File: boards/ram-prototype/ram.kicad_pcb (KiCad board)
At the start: 4 copper layers, 165 x 141 mm, 630 parts, among them J1 PinHeader_1x24_P2.54mm_Vertic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, J2 PinHeader_1x04_P2.54mm_Vertic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, J3 PinHeader_1x14_P2.54mm_Vertic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, J4 PinHeader_1x16_P2.54mm_Vertic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, J5 Molex_Mini-Fit_Jr_5566-08A_2x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, U1 DSBGA\-5_NumericPads, U10 DSBGA\-5_NumericPads, U100 DSBGA\-5_NumericPads, U101 DSBGA\-5_NumericPads, U102 DSBGA\-5_NumericPads, U103 DSBGA\-5_NumericPads, U104 DSBGA\-5_NumericPads, U105 DSBGA\-5_NumericPads, U106 DSBGA\-5_NumericPads, U107 DSBGA\-5_NumericPads, U108 DSBGA\-5_NumericPads, U109 DSBGA\-5_NumericPads, U11 DSBGA\-5_NumericPads, U110 DSBGA\-5_NumericPads, U111 DSBGA\-5_NumericPads, U112 DSBGA\-5_NumericPads, U113 DSBGA\-5_NumericPads, U114 DSBGA\-5_NumericPads, U115 DSBGA\-5_NumericPads, U116 DSBGA\-5_NumericPads, U117 DSBGA\-5_NumericPads, U118 DSBGA\-5_NumericPads, U119 DSBGA\-5_NumericPads, U12 DSBGA\-5_NumericPads, U120 DSBGA\-5_NumericPads, U121 DSBGA\-5_NumericPads, U122 DSBGA\-5_NumericPads, U123 DSBGA\-5_NumericPads, U124 DSBGA\-5_NumericPads, U125 DSBGA\-5_NumericPads, U126 DSBGA\-5_NumericPads, U127 DSBGA\-5_NumericPads, U128 DSBGA\-5_NumericPads, U129 DSBGA\-5_NumericPads, U13 DSBGA\-5_NumericPads, U130 DSBGA\-5_NumericPads, U131 DSBGA\-5_NumericPads, U132 DSBGA\-5_NumericPads, U133 DSBGA\-5_NumericPads, U134 DSBGA\-5_NumericPads, U135 DSBGA\-5_NumericPads, U136 DSBGA\-5_NumericPads, U137 DSBGA\-5_NumericPads, U138 DSBGA\-5_NumericPads, U139 DSBGA\-5_NumericPads, U14 DSBGA\-5_NumericPads, U140 DSBGA\-5_NumericPads, U141 DSBGA\-5_NumericPads, U142 DSBGA\-5_NumericPads, U143 DSBGA\-5_NumericPads, U144 DSBGA\-5_NumericPads, U145 DSBGA\-5_NumericPads, U146 DSBGA\-5_NumericPads, U147 DSBGA\-5_NumericPads, U148 DSBGA\-5_NumericPads, U149 DSBGA\-5_NumericPads, U15 DSBGA\-5_NumericPads, U150 DSBGA\-5_NumericPads, U151 DSBGA\-5_NumericPads, U152 DSBGA\-5_NumericPads, U153 DSBGA\-5_NumericPads, U154 DSBGA\-5_NumericPads, U155 DSBGA\-5_NumericPads, U156 DSBGA\-5_NumericPads, U157 DSBGA\-5_NumericPads, U158 DSBGA\-5_NumericPads, U159 DSBGA\-5_NumericPads, U16 DSBGA\-5_NumericPads, U160 DSBGA\-5_NumericPads, U161 DSBGA\-5_NumericPads, U162 DSBGA\-5_NumericPads, U163 DSBGA\-5_NumericPads, U164 DSBGA\-5_NumericPads, U165 DSBGA\-5_NumericPads, U166 DSBGA\-5_NumericPads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

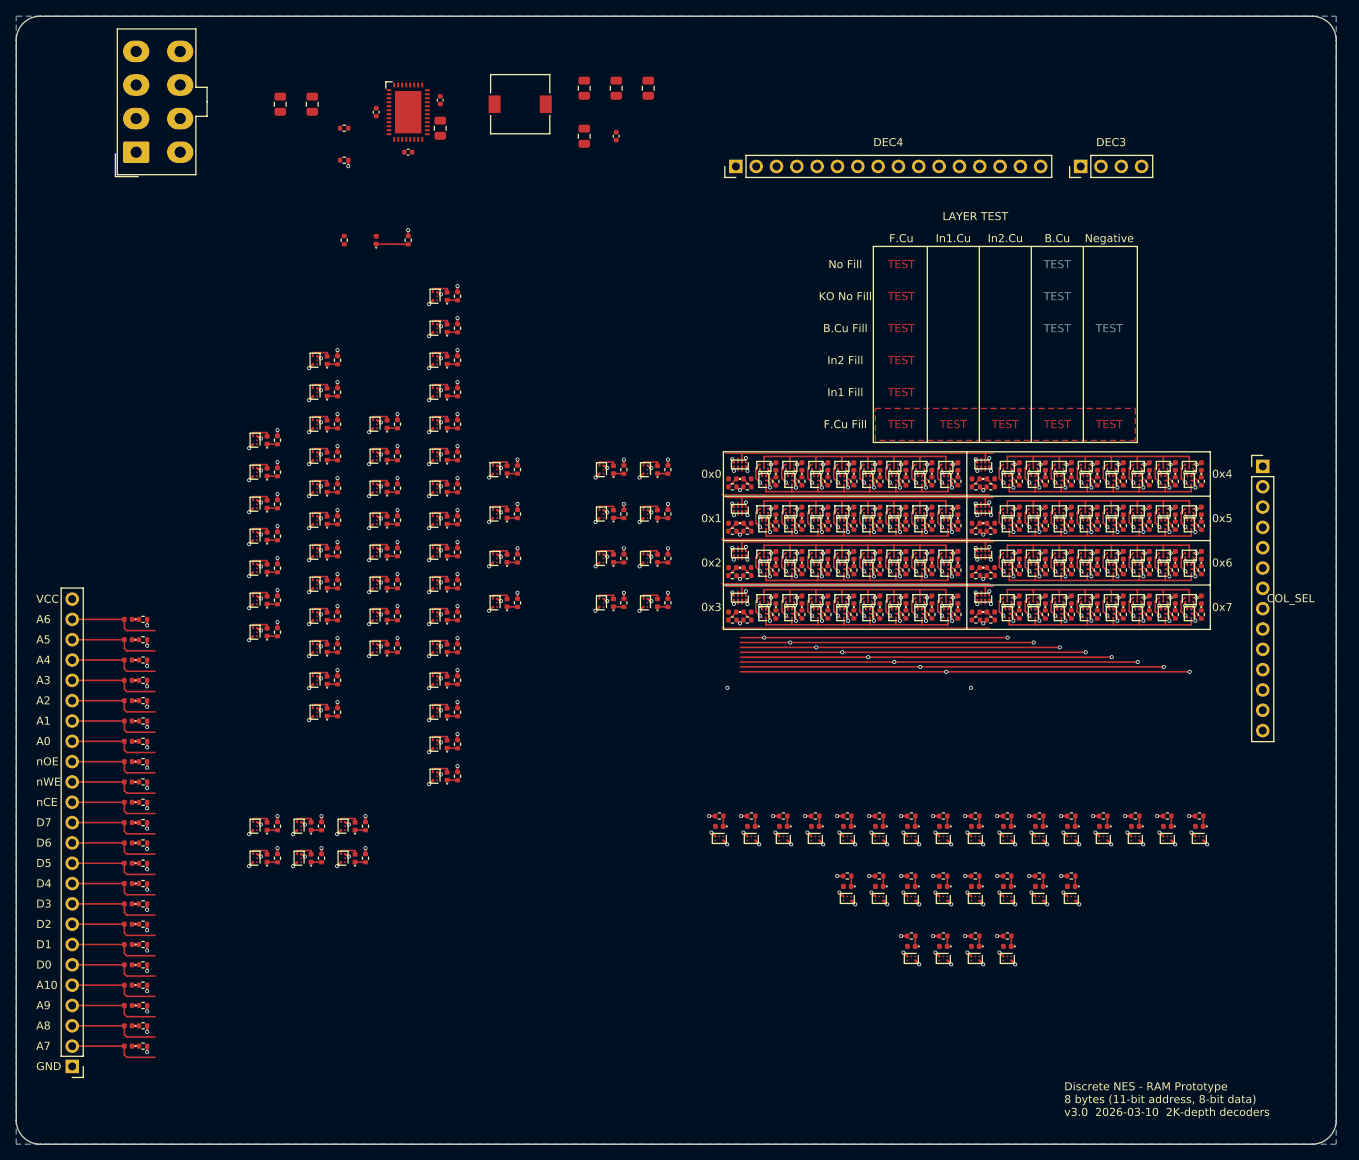
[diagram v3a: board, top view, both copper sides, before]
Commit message: add copper pours, thermal vias, and SW keepout for power supply layout
Rotates TPS546D24A 180° so PVIN faces input caps (left) and SW faces
inductor (right), matching datasheet layout recommendation (Fig 10-1).

Copper pours (F.Cu, regional):
- PVIN pour: input caps to PVIN pins, solid pad connection
- PGND pour: around thermal pad, connects vias to PGND pins
- VOUT pour: inductor output through output caps to VCC
- SW keepout zone: prevents fill in switching node area

Thermal vias: 2x3 grid (6 vias, 0.3mm drill) under exposed pad,
connecting F.Cu to B.Cu GND plane per datasheet land pattern.

Bypass caps repositioned for 180° IC rotation:
- C3 (PVIN HF) + C5 (VDD5): left side near respective pins
- C4 (BOOT) + C6 (BP1V5): right side near SW/BOOT area

Default DRC: 0 errors, 0 warnings.

Co-Authored-By: Claude Opus 4.6 (1M context) <noreply@anthropic.com>
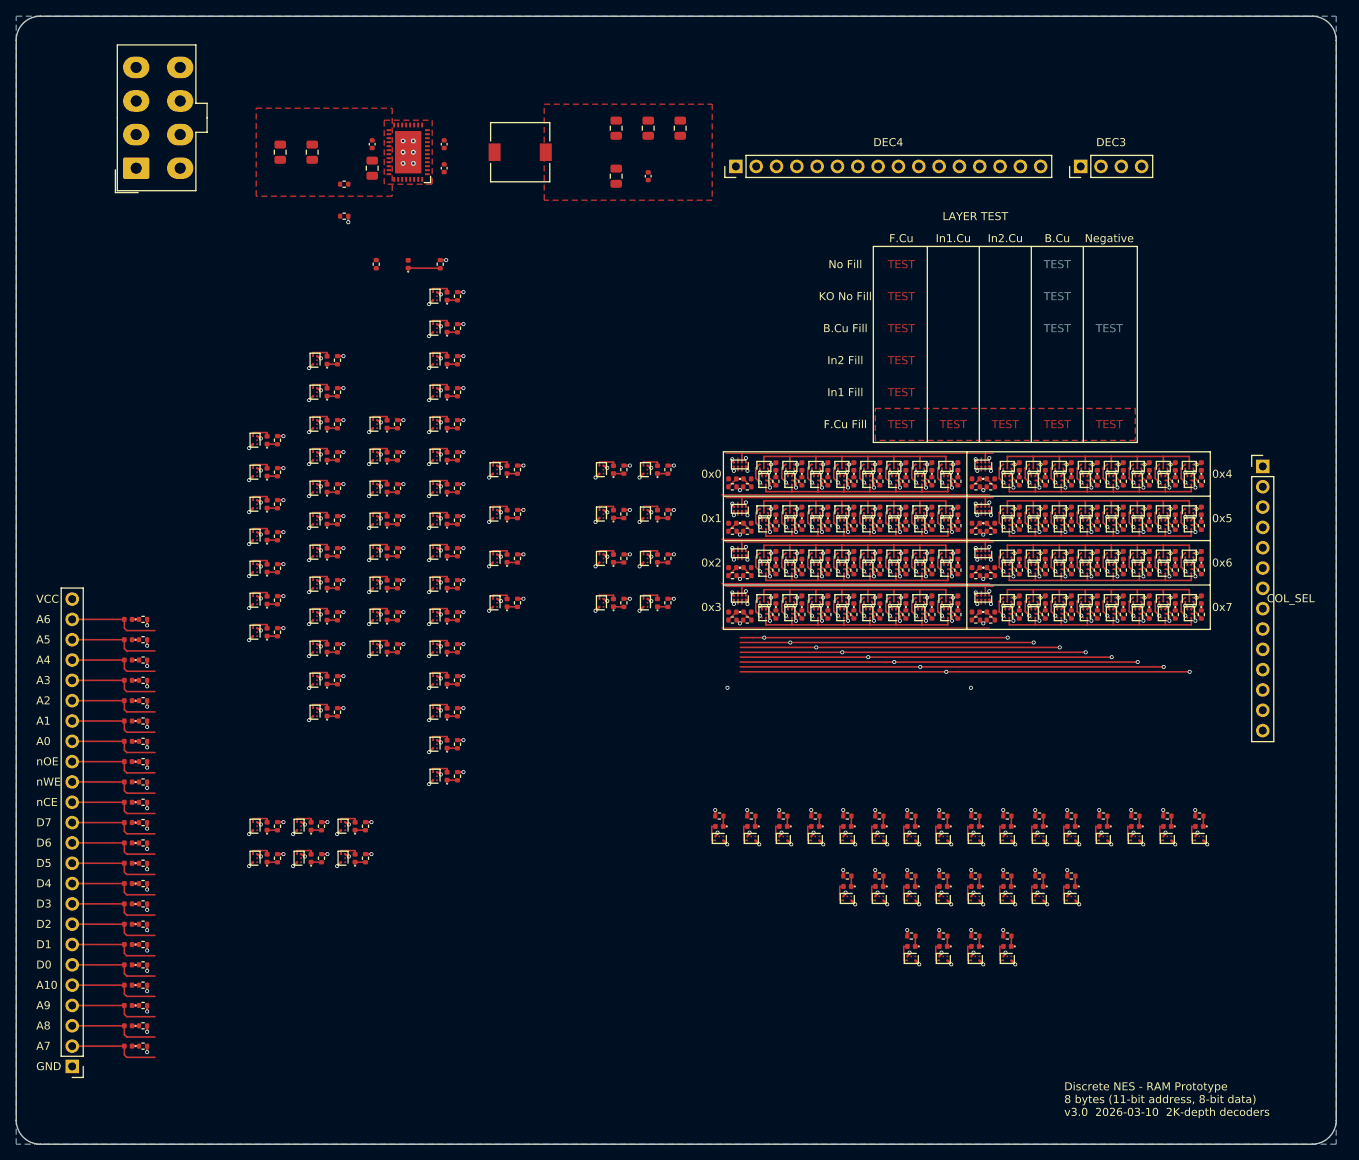
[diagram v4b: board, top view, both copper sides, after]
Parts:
- moved C5 9.86 mm to (57.5, 32.0)
- moved R192 7.00 mm to (54.0, 34.0)
- moved R193 7.00 mm to (54.0, 38.0)
- moved C10 6.40 mm to (88.0, 33.0)
- moved C11 6.40 mm to (92.0, 33.0)
- moved C7 6.40 mm to (88.0, 27.0)
- moved C8 6.40 mm to (92.0, 27.0)
- moved C9 6.40 mm to (96.0, 27.0)
- moved C1 6.00 mm to (46.0, 30.0)
- moved C2 6.00 mm to (50.0, 30.0)
- moved L1 6.00 mm to (76.0, 30.0)
- moved C4 5.52 mm to (66.5, 29.0)
- moved D192 5.00 mm to (62.0, 44.0)
- moved R194 5.00 mm to (58.0, 44.0)
- moved R195 5.00 mm to (66.0, 44.0)
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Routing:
- net GND: track 353.6 -> 349.7 mm, vias 282 -> 288
- net Net-(D70-A): track 0.00 -> 2.67 mm
- net /Column Select/GA2: track 0.00 -> 2.67 mm
- net /Column Select/GA1: track 0.00 -> 2.67 mm
- net /Column Select/GA0: track 0.00 -> 2.67 mm
- net /COL_SEL_6: track 0.00 -> 2.67 mm
- net /COL_SEL_5: track 0.00 -> 2.67 mm
- net /COL_SEL_4: track 0.00 -> 2.67 mm
- net /COL_SEL_3: track 0.00 -> 2.67 mm
- net /COL_SEL_2: track 0.00 -> 2.67 mm
- net /COL_SEL_1: track 43.6 -> 46.3 mm
- net /COL_SEL_0: track 43.6 -> 46.3 mm
- net Net-(D73-A): track 0.00 -> 2.66 mm
- net Net-(D72-A): track 0.00 -> 2.66 mm
- net Net-(D71-A): track 0.00 -> 2.66 mm
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- added copper zone on F.Cu, net /Power Supply/+12V
- added copper zone on F.Cu, net VCC

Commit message: stack row_ctrl write/read AND gates vertically with 45° enable bus routing
- Row control layout changed from side-by-side to vertically stacked
  (2.3mm spacing between write and read AND gate centers)
- WRITE_EN: 45° diagonal up-right from LED junction to bus
- READ_EN: corridor route (45° up-right, horizontal past R/GND via,
  45° diagonal down-right to bus)
- Row_ctrl-to-RAM gap reduced from 3.0mm to 1.0mm
- Board width reduced from 233mm to 158mm

Co-Authored-By: Claude Opus 4.6 (1M context) <noreply@anthropic.com>
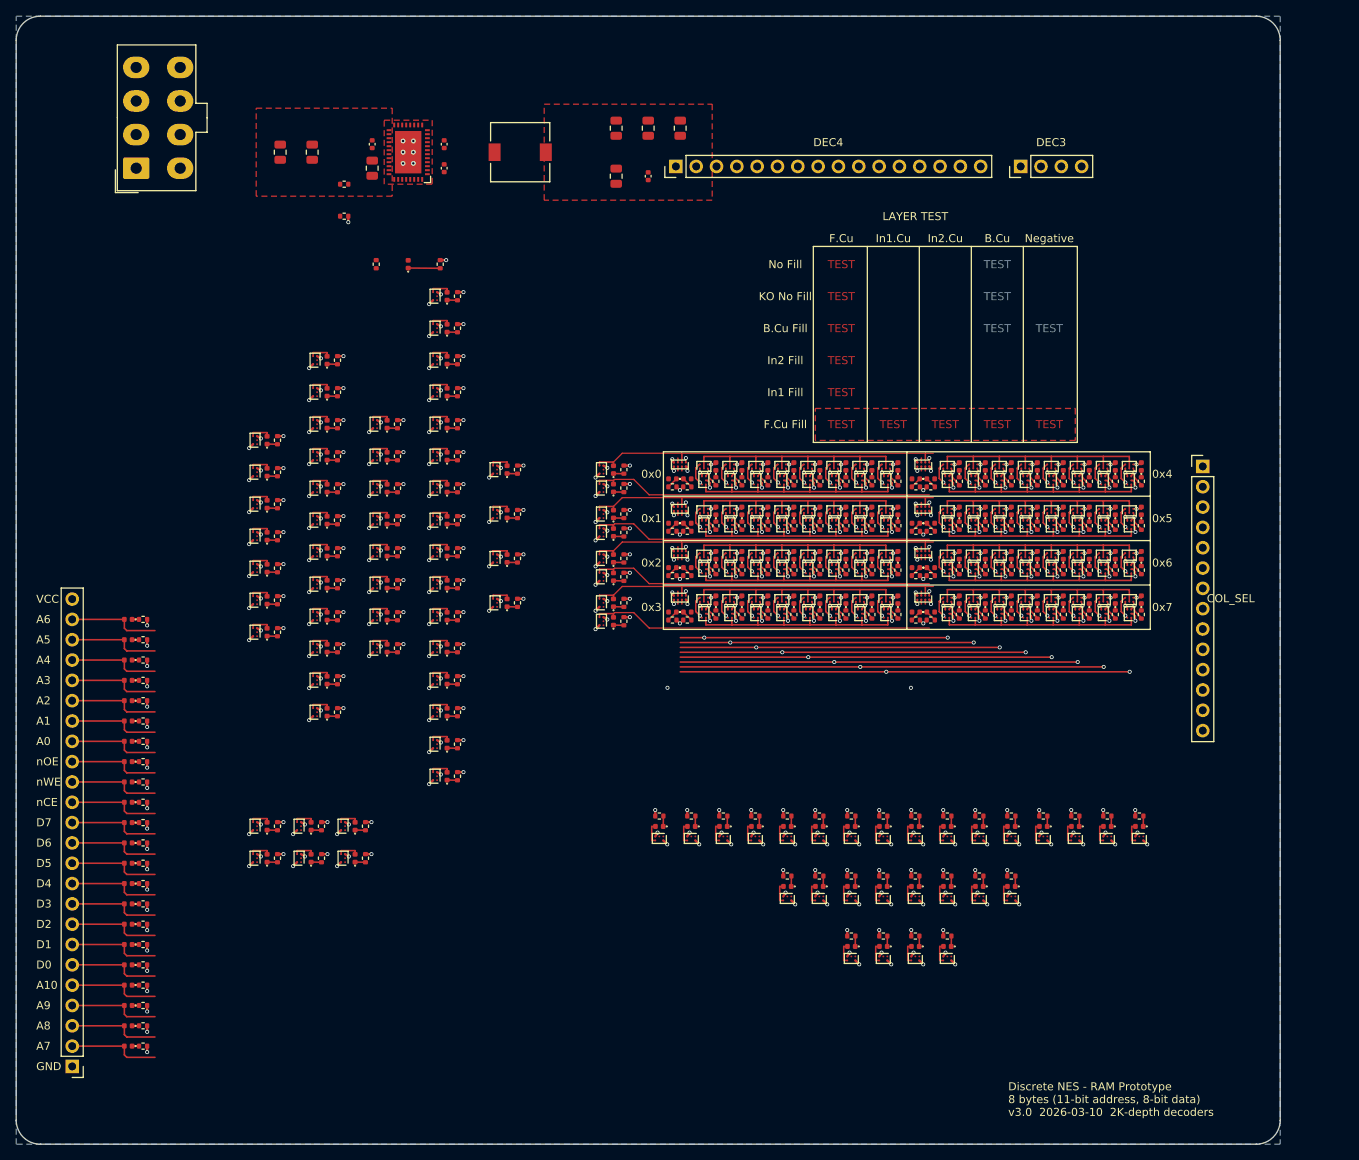
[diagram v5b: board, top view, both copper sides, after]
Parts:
- moved D124 7.50 mm to (125.5, 70.8)
- moved D125 7.50 mm to (125.5, 76.4)
- moved D126 7.50 mm to (125.5, 81.9)
- moved D127 7.50 mm to (125.5, 87.5)
- moved D128 7.50 mm to (123.2, 69.3)
- moved D129 7.50 mm to (123.2, 74.8)
- moved D130 7.50 mm to (123.2, 80.4)
- moved D131 7.50 mm to (123.2, 85.9)
- moved R124 7.50 mm to (125.5, 71.8)
- moved R125 7.50 mm to (125.5, 77.4)
- moved R126 7.50 mm to (125.5, 82.9)
- moved R127 7.50 mm to (125.5, 88.5)
- moved R128 7.50 mm to (123.2, 71.1)
- moved R129 7.50 mm to (123.2, 76.7)
- moved R130 7.50 mm to (123.2, 82.2)
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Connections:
- net /Power Supply/BOOT_INT renamed Net-(U226-BOOT)
- net /Power Supply/BP1V5_INT renamed Net-(U226-BP1V5)
- net /Power Supply/PGOOD renamed Net-(D192-A)
- net /Power Supply/VDD5_INT renamed Net-(U226-VDD5)
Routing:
- net /WRITE_EN_ROW_0: track 38.4 -> 45.4 mm
- net /WRITE_EN_ROW_3: track 38.4 -> 45.4 mm
- net /WRITE_EN_ROW_2: track 38.4 -> 45.4 mm
- net /WRITE_EN_ROW_1: track 38.4 -> 45.4 mm
- net /READ_EN_ROW_1: track 37.2 -> 44.1 mm
- net /READ_EN_ROW_0: track 37.2 -> 44.1 mm
- net /READ_EN_ROW_3: track 37.2 -> 44.1 mm
- net /READ_EN_ROW_2: track 37.2 -> 44.1 mm
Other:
- board size 165 x 141 mm -> 158 x 141 mm

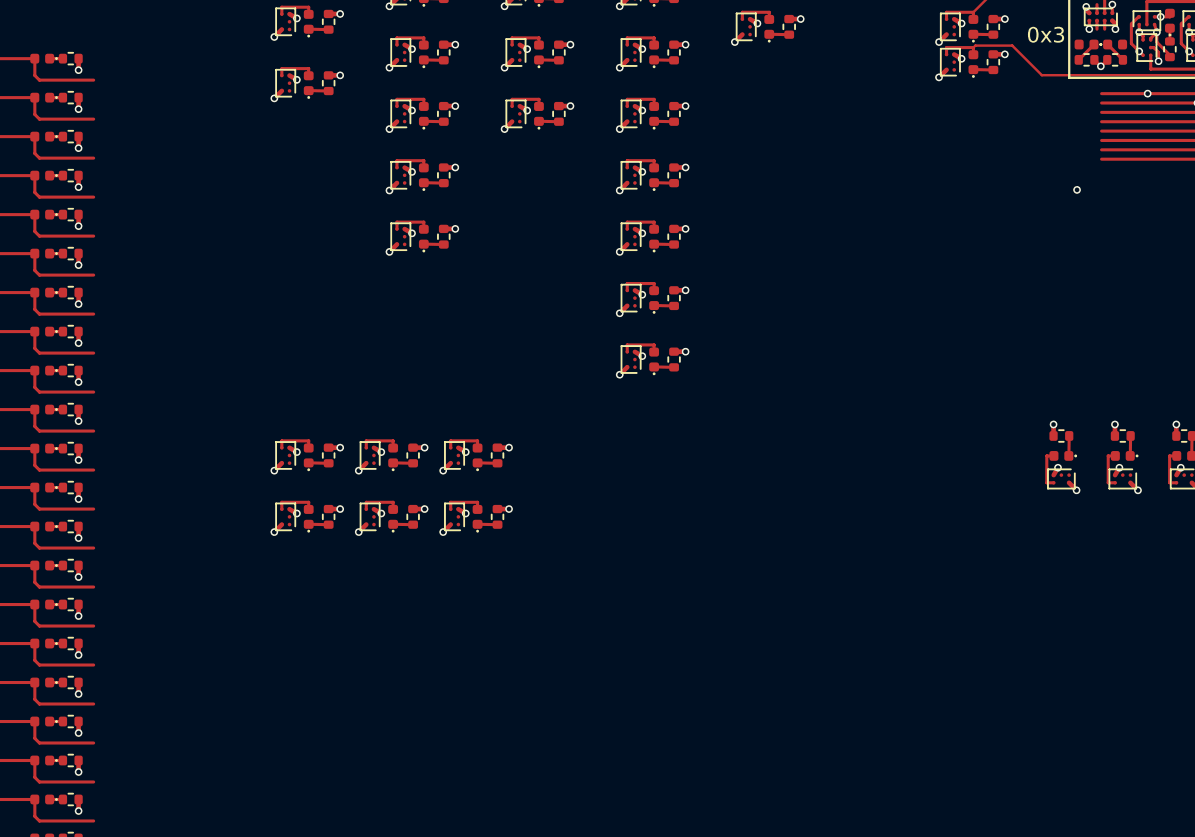
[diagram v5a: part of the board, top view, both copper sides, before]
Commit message: route D* data bus from byte grid fanout to connector on F.Cu
Add preroute_dbus_to_connector() that routes all 8 D-bus signals
from the byte grid fanout to the connector LED stubs entirely on
F.Cu, going around the address decoder and control logic groups.

Route geometry per signal:
- Staggered horizontal extension (fans traces for 0.61mm diagonal
  perpendicular spacing via 0.253mm X-stagger per trace)
- 45° diagonal DOWN-LEFT from byte grid to bus corridor below
  control logic (y≈121-125)
- Natural peel-off transition to horizontal bus at 0.61mm spacing
- Horizontal bus LEFT through clear corridor
- Chamfered 45° fan to connector stub endpoints

Automatic via avoidance scans existing COL_SEL fanout vias and
shifts diagonal lines to maintain clearance. No board size change
needed (158x141mm unchanged). No new DRC errors introduced.

Co-Authored-By: Claude Opus 4.6 (1M context) <noreply@anthropic.com>
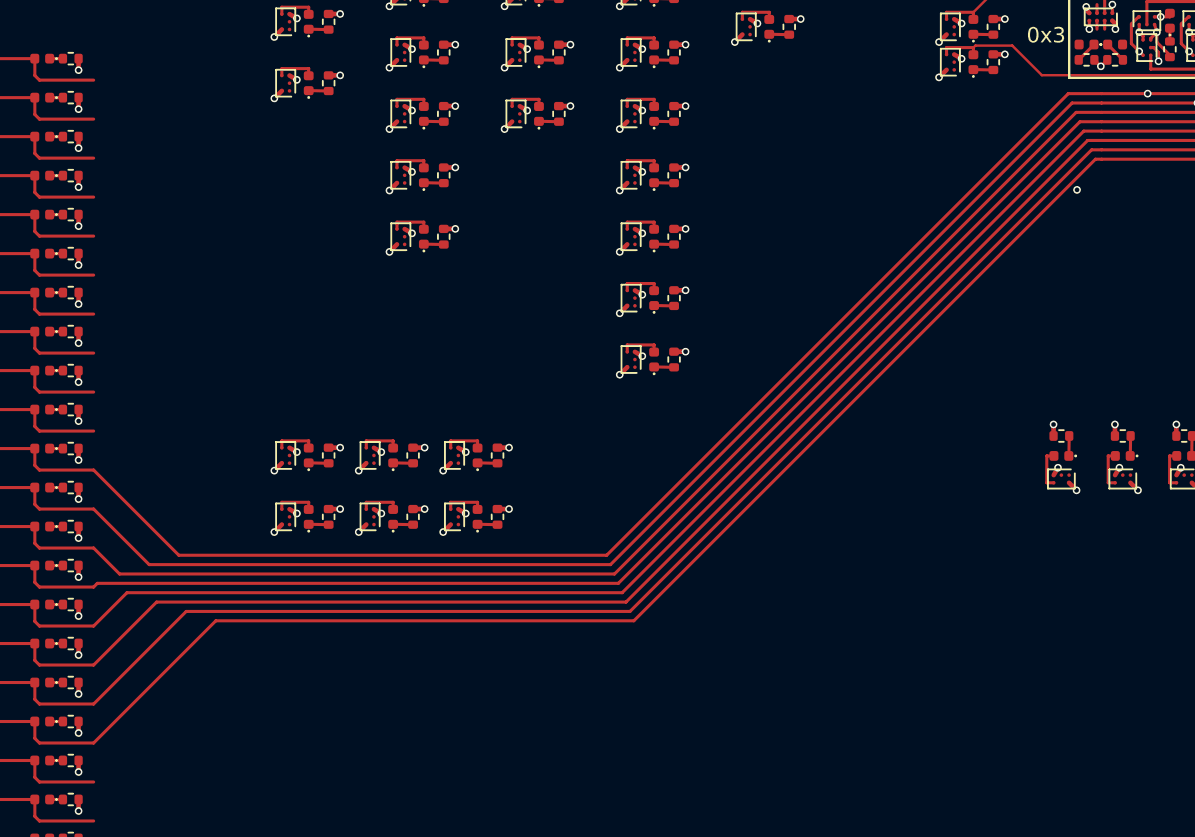
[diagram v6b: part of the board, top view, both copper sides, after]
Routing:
- net /D0: track 130.8 -> 212.2 mm
- net /D1: track 126.4 -> 207.0 mm
- net /D7: track 99.5 -> 179.9 mm
- net /D2: track 121.9 -> 201.7 mm
- net /D6: track 104.0 -> 183.6 mm
- net /D3: track 117.4 -> 196.4 mm
- net /D5: track 108.5 -> 187.3 mm
- net /D4: track 112.9 -> 191.2 mm
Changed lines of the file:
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@@
   (segment (start 124.84 86.48) (end 124.84 96.95) (width 0.2) (layer "In1.Cu") (net 37))
   (via (at 124.84 96.95) (size 0.5) (drill 0.3) (layers "F.Cu" "In1.Cu") (net 37))
+  (segment (start 96.01 90.68) (end 93.84 90.68) (width 0.2) (layer "F.Cu") (net 71))
+  (segment (start 93.84 90.68) (end 63.77 120.75) (width 0.2) (layer "F.Cu") (net 71))
+  (segment (start 63.77 120.75) (end 35.9 120.75) (width 0.2) (layer "F.Cu") (net 71))
+  (segment (start 35.9 120.75) (end 30.35 115.2) (width 0.2) (layer "F.Cu") (net 71))
+  (segment (start 96.01 91.29) (end 94.09 91.29) (width 0.2) (layer "F.Cu") (net 70))
+  (segment (start 94.09 91.29) (end 64.02 121.36) (width 0.2) (layer "F.Cu") (net 70))
+  (segment (start 64.02 121.36) (end 33.97 121.36) (width 0.2) (layer "F.Cu") (net 70))
+  (segment (start 33.97 121.36) (end 30.35 117.74) (width 0.2) (layer "F.Cu") (net 70))
+  (segment (start 96.01 91.9) (end 94.35 91.9) (width 0.2) (layer "F.Cu") (net 69))
+  (segment (start 94.35 91.9) (end 64.28 121.97) (width 0.2) (layer "F.Cu") (net 69))
+  (segment (start 64.28 121.97) (end 32.04 121.97) (width 0.2) (layer "F.Cu") (net 69))
+  (segment (start 32.04 121.97) (end 30.35 120.28) (width 0.2) (layer "F.Cu") (net 69))
+  (segment (start 96.01 92.51) (end 94.6 92.51) (width 0.2) (layer "F.Cu") (net 68))
+  (segment (start 94.6 92.51) (end 64.53 122.58) (width 0.2) (layer "F.Cu") (net 68))
+  (segment (start 64.53 122.58) (end 30.59 122.58) (width 0.2) (layer "F.Cu") (net 68))
+  (segment (start 30.59 122.58) (end 30.35 122.82) (width 0.2) (layer "F.Cu") (net 68))
+  (segment (start 96.01 93.12) (end 94.85 93.12) (width 0.2) (layer "F.Cu") (net 67))
+  (segment (start 94.85 93.12) (end 64.78 123.19) (width 0.2) (layer "F.Cu") (net 67))
+  (segment (start 64.78 123.19) (end 32.52 123.19) (width 0.2) (layer "F.Cu") (net 67))
+  (segment (start 32.52 123.19) (end 30.35 125.36) (width 0.2) (layer "F.Cu") (net 67))
+  (segment (start 96.01 93.73) (end 95.1 93.73) (width 0.2) (layer "F.Cu") (net 66))
+  (segment (start 95.1 93.73) (end 65.03 123.8) (width 0.2) (layer "F.Cu") (net 66))
+  (segment (start 65.03 123.8) (end 34.45 123.8) (width 0.2) (layer "F.Cu") (net 66))
+  (segment (start 34.45 123.8) (end 30.35 127.9) (width 0.2) (layer "F.Cu") (net 66))
+  (segment (start 96.01 94.34) (end 95.36 94.34) (width 0.2) (layer "F.Cu") (net 65))
+  (segment (start 95.36 94.34) (end 65.29 124.41) (width 0.2) (layer "F.Cu") (net 65))
+  (segment (start 65.29 124.41) (end 36.38 124.41) (width 0.2) (layer "F.Cu") (net 65))
+  (segment (start 36.38 124.41) (end 30.35 130.44) (width 0.2) (layer "F.Cu") (net 65))
+  (segment (start 96.01 94.95) (end 95.61 94.95) (width 0.2) (layer "F.Cu") (net 64))
+  (segment (start 95.61 94.95) (end 65.54 125.02) (width 0.2) (layer "F.Cu") (net 64))
+  (segment (start 65.54 125.02) (end 38.31 125.02) (width 0.2) (layer "F.Cu") (net 64))
+  (segment (start 38.31 125.02) (end 30.35 132.98) (width 0.2) (layer "F.Cu") (net 64))
   (zone (net 91) (net_name "/Power Supply/+12V") (layer "F.Cu") (hatch edge 0.508)
     (priority 1)
